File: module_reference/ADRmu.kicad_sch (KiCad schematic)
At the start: 7 parts, among them J101 Harting 09042326831, J102 10Vf, J103 10Vs, J104 7Vref, J105 Lo

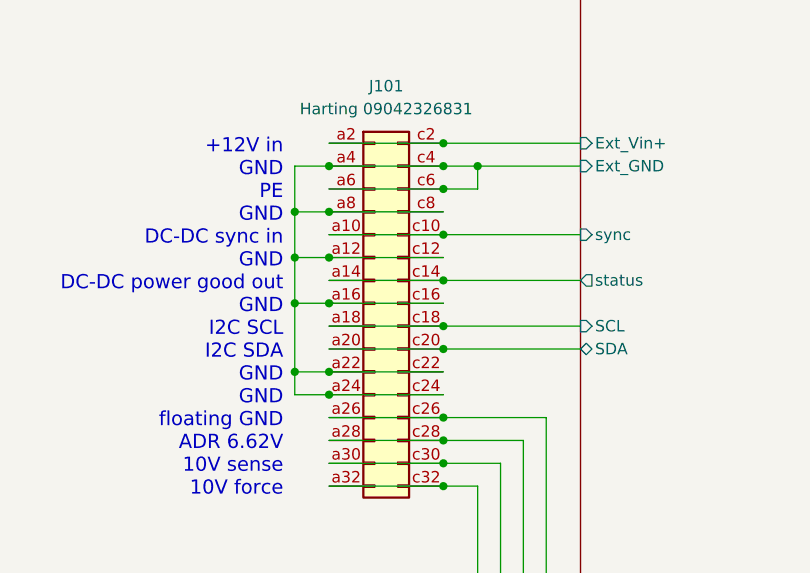
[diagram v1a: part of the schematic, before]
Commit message: backplane connector changes
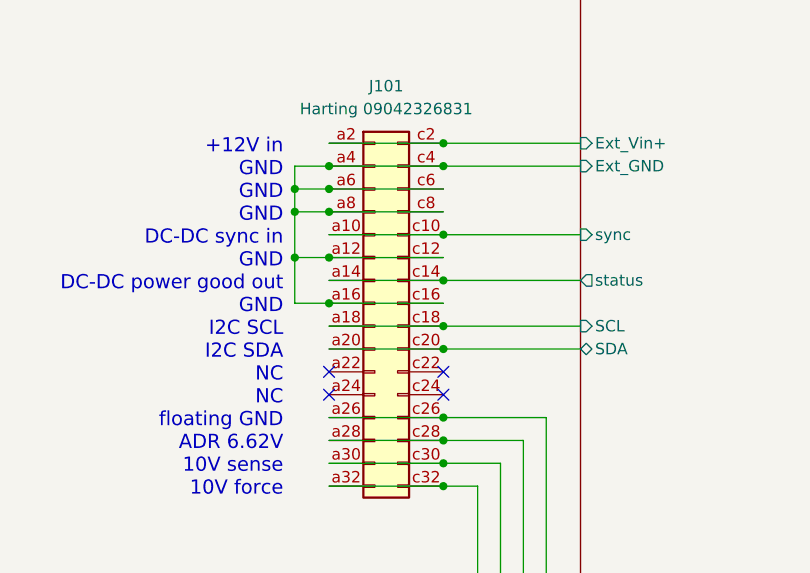
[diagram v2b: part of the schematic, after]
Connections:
- net DC-DC/Ext_GND: no longer J101.a22 (Pin_a22), J101.a24 (Pin_a24), J101.c22 (Pin_c22), J101.c24 (Pin_c24)
- no-connect marks 0 -> 4
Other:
- note added: "+12V in GND GND GND DC-DC sync in GND DC-DC power good out GND I2C SCL I2C SDA NC NC floating GND ADR 6.62V 10V sense 10V force"
- note removed: "+12V in GND PE GND DC-DC sync in GND DC-DC power good out GND I2C SCL I2C SDA GND GND floating GND ADR 6.62V 10V sense 10V force"
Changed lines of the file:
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@@
   (junction (at 55.88 92.71) (diameter 0) (color 0 0 0 0)
   )
-  (junction (at 55.88 100.33) (diameter 0) (color 0 0 0 0)
-  )
   (junction (at 228.6 71.12) (diameter 0) (color 0 0 0 0)
   )
@@
   (junction (at 68.58 97.79) (diameter 0) (color 0 0 0 0)
   )
-  (junction (at 52.07 100.33) (diameter 0) (color 0 0 0 0)
+  (junction (at 55.88 80.01) (diameter 0) (color 0 0 0 0)
   )
   (junction (at 52.07 87.63) (diameter 0) (color 0 0 0 0)
@@
   (junction (at 228.6 116.84) (diameter 0) (color 0 0 0 0)
   )
-  (junction (at 72.39 77.47) (diameter 0) (color 0 0 0 0)
-  )
   (junction (at 55.88 77.47) (diameter 0) (color 0 0 0 0)
   )
@@
   (junction (at 68.58 113.03) (diameter 0) (color 0 0 0 0)
   )
-  (junction (at 52.07 92.71) (diameter 0) (color 0 0 0 0)
-  )
-  (junction (at 68.58 80.01) (diameter 0) (color 0 0 0 0)
+  (junction (at 52.07 80.01) (diameter 0) (color 0 0 0 0)
   )
   (junction (at 68.58 95.25) (diameter 0) (color 0 0 0 0)
@@
   (junction (at 223.52 55.88) (diameter 0) (color 0 0 0 0)
   )
-  (junction (at 55.88 102.87) (diameter 0) (color 0 0 0 0)
-  )
+  (no_connect (at 55.88 102.87))
+  (no_connect (at 55.88 100.33))
+  (no_connect (at 68.58 100.33))
+  (no_connect (at 68.58 102.87))
   (wire (pts (xy 245.11 156.21) (xy 74.93 156.21))
     (stroke (width 0) (type default) (color 0 0 0 0))
@@
     (stroke (width 0) (type default) (color 0 0 0 0))
   )
-  (wire (pts (xy 52.07 100.33) (xy 55.88 100.33))
+  (wire (pts (xy 52.07 80.01) (xy 55.88 80.01))
     (stroke (width 0) (type default) (color 0 0 0 0))
   )
@@
     (stroke (width 0) (type default) (color 0 0 0 0))
   )
-  (wire (pts (xy 52.07 77.47) (xy 52.07 82.55))
+  (wire (pts (xy 52.07 77.47) (xy 52.07 80.01))
     (stroke (width 0) (type default) (color 0 0 0 0))
   )
@@
     (stroke (width 0) (type default) (color 0 0 0 0))
   )
+  (wire (pts (xy 52.07 80.01) (xy 52.07 82.55))
+    (stroke (width 0) (type default) (color 0 0 0 0))
+  )
   (wire (pts (xy 55.88 77.47) (xy 68.58 77.47))
     (stroke (width 0) (type default) (color 0 0 0 0))
@@
     (stroke (width 0) (type default) (color 0 0 0 0))
   )
-  (wire (pts (xy 55.88 102.87) (xy 68.58 102.87))
-    (stroke (width 0) (type default) (color 0 0 0 0))
-  )
   (wire (pts (xy 215.9 116.84) (xy 228.6 116.84))
     (stroke (width 0) (type default) (color 0 0 0 0))
@@
     (stroke (width 0) (type default) (color 0 0 0 0))
   )
-  (wire (pts (xy 52.07 92.71) (xy 52.07 100.33))
-    (stroke (width 0) (type default) (color 0 0 0 0))
-  )
   (wire (pts (xy 77.47 153.67) (xy 242.57 153.67))
     (stroke (width 0) (type default) (color 0 0 0 0))
@@
     (stroke (width 0) (type default) (color 0 0 0 0))
   )
-  (wire (pts (xy 52.07 100.33) (xy 52.07 102.87))
-    (stroke (width 0) (type default) (color 0 0 0 0))
-  )
   (wire (pts (xy 52.07 92.71) (xy 55.88 92.71))
     (stroke (width 0) (type default) (color 0 0 0 0))
@@
     (stroke (width 0) (type default) (color 0 0 0 0))
   )
-  (wire (pts (xy 72.39 80.01) (xy 72.39 77.47))
-    (stroke (width 0) (type default) (color 0 0 0 0))
-  )
   (wire (pts (xy 149.86 151.13) (xy 80.01 151.13))
     (stroke (width 0) (type default) (color 0 0 0 0))
@@
     (stroke (width 0) (type default) (color 0 0 0 0))
   )
-  (wire (pts (xy 52.07 102.87) (xy 55.88 102.87))
-    (stroke (width 0) (type default) (color 0 0 0 0))
-  )
   (wire (pts (xy 55.88 85.09) (xy 68.58 85.09))
     (stroke (width 0) (type default) (color 0 0 0 0))
@@
     (stroke (width 0) (type default) (color 0 0 0 0))
   )
-  (wire (pts (xy 72.39 77.47) (xy 83.82 77.47))
+  (wire (pts (xy 68.58 77.47) (xy 83.82 77.47))
     (stroke (width 0) (type default) (color 0 0 0 0))
   )
@@
     (stroke (width 0) (type default) (color 0 0 0 0))
   )
-  (wire (pts (xy 55.88 100.33) (xy 68.58 100.33))
-    (stroke (width 0) (type default) (color 0 0 0 0))
-  )
   (wire (pts (xy 223.52 104.14) (xy 223.52 151.13))
     (stroke (width 0) (type default) (color 0 0 0 0))
@@
     (stroke (width 0) (type default) (color 0 0 0 0))
   )
+  (wire (pts (xy 68.58 107.95) (xy 77.47 107.95))
+    (stroke (width 0) (type default) (color 0 0 0 0))
+  )
   (wire (pts (xy 55.88 80.01) (xy 68.58 80.01))
     (stroke (width 0) (type default) (color 0 0 0 0))
   )
-  (wire (pts (xy 68.58 107.95) (xy 77.47 107.95))
-    (stroke (width 0) (type default) (color 0 0 0 0))
-  )
-  (wire (pts (xy 68.58 80.01) (xy 72.39 80.01))
-    (stroke (width 0) (type default) (color 0 0 0 0))
-  )
   (wire (pts (xy 68.58 110.49) (xy 74.93 110.49))
     (stroke (width 0) (type default) (color 0 0 0 0))
@@
     (stroke (width 0) (type default) (color 0 0 0 0))
   )
-  (wire (pts (xy 68.58 77.47) (xy 72.39 77.47))
-    (stroke (width 0) (type default) (color 0 0 0 0))
-  )
   (wire (pts (xy 223.52 55.88) (xy 223.52 96.52))
     (stroke (width 0) (type default) (color 0 0 0 0))
@@
     (stroke (width 0) (type default) (color 0 0 0 0))
   )
-  (text "+12V in\nGND\nPE\nGND\nDC-DC sync in\nGND\nDC-DC power good out\nGND\nI2C SCL\nI2C SDA\nGND\nGND\nfloating GND\nADR 6.62V\n10V sense\n10V force"
+  (text "+12V in\nGND\nGND\nGND\nDC-DC sync in\nGND\nDC-DC power good out\nGND\nI2C SCL\nI2C SDA\nNC\nNC\nfloating GND\nADR 6.62V\n10V sense\n10V force"
     (at 50.8 114.3 0)
     (effects (font (size 1.5748 1.5748)) (justify right bottom))

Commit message: asdf
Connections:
- net DC-DC/Ext_GND: no longer J101.a16 (Pin_a16), J101.a6 (Pin_a6), J101.a8 (Pin_a8), J101.c16 (Pin_c16), J101.c6 (Pin_c6), J101.c8 (Pin_c8)
- net DC-DC/SCL: now also J101.a16 (Pin_a16), J101.c16 (Pin_c16); no longer J101.a18 (Pin_a18), J101.c18 (Pin_c18)
- net DC-DC/SDA: now also J101.a18 (Pin_a18), J101.c18 (Pin_c18); no longer J101.a20 (Pin_a20), J101.c20 (Pin_c20)
- no-connect marks 4 -> 10
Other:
- note added: "+12V in 0V in NC NC DC-DC sync in GND DC-DC power good out I2C SCL I2C SDA NC NC NC floating GND ADR 6.62V 10V sense 10V force"
- note removed: "+12V in GND GND GND DC-DC sync in GND DC-DC power good out GND I2C SCL I2C SDA NC NC floating GND ADR 6.62V 10V sense 10V force"

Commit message: rev 0.4 layout step
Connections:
- net DC-DC/status: no longer J101.a14 (Pin_a14), J101.c14 (Pin_c14)
- net Earth: now reaches J101.a24 (Pin_a24)
- net Earth: now also J101.c24 (Pin_c24)
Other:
- note added: "+12V in 0V in NC NC DC-DC sync in GND NC I2C SCL I2C SDA NC NC PE floating GND ADR 6.62V 10V sense 10V force"
- note removed: "+12V in 0V in NC NC DC-DC sync in GND DC-DC power good out I2C SCL I2C SDA NC NC NC floating GND ADR 6.62V 10V sense 10V force"
